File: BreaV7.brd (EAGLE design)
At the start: 30.8 x 19 mm, 32 parts, among them J2 XF2L-0535-1, J3 XF2L-0635-1, Q1 ABM-16MHZ, SW1 LS12T2-T, SW2 EVQ11U09K, SW3 ESE31L11T, U2 TPS62200, X1 22-23-2021

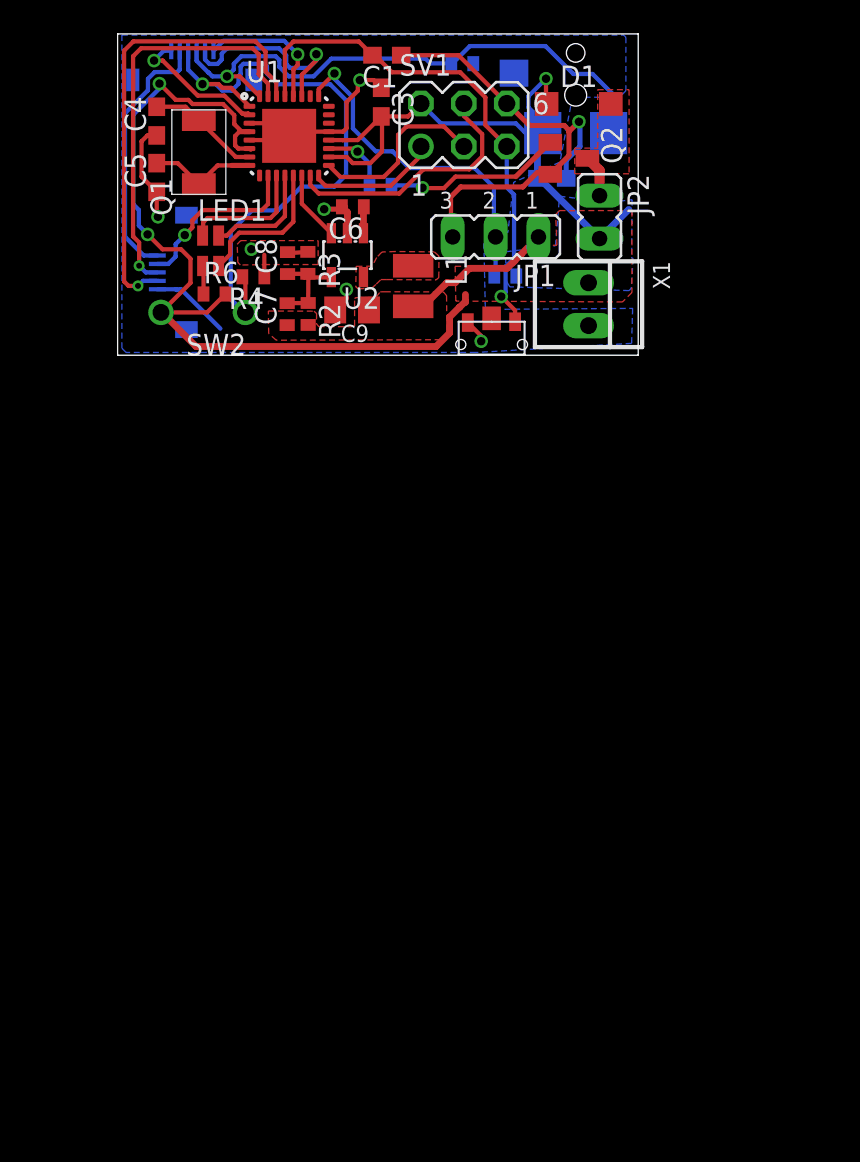
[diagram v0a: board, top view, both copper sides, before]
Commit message: Combined boards
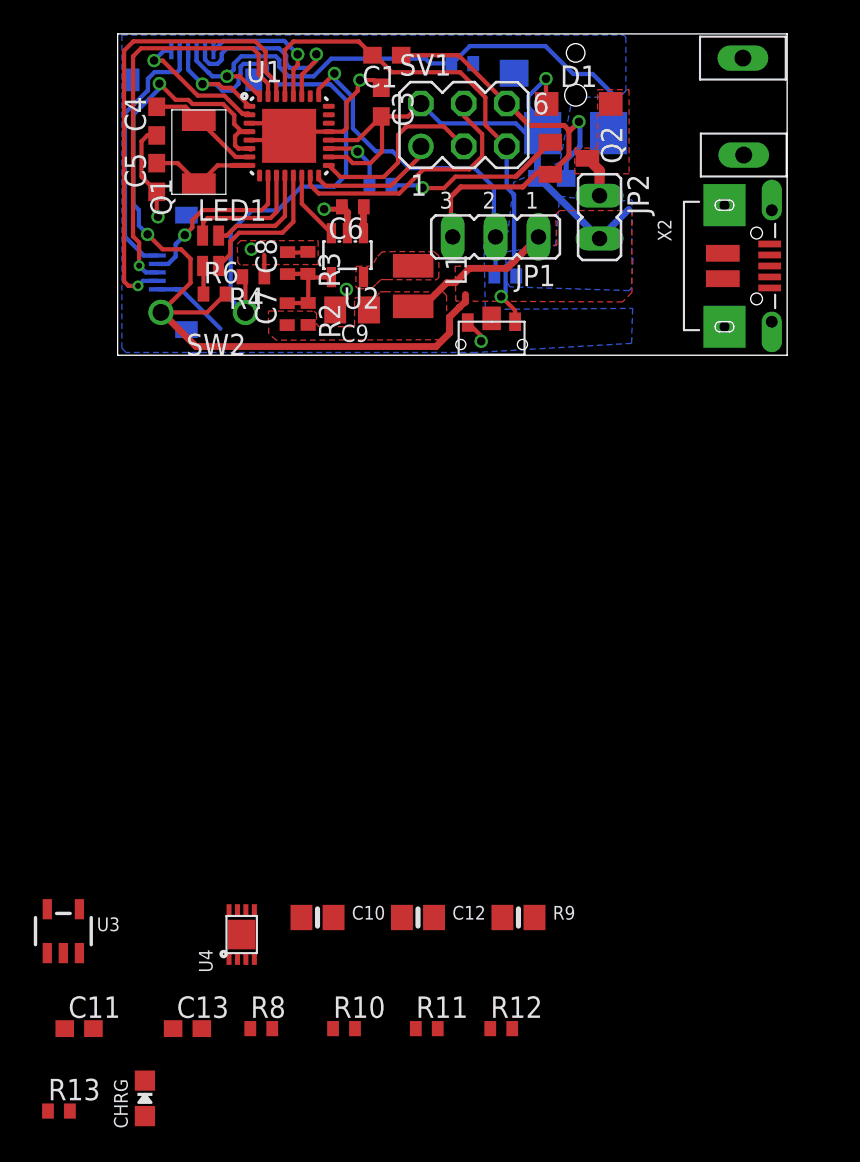
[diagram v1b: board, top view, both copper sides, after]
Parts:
- added C10, C12: 10µF, microbuilder:0805-NO
- added C11: 10nF, rcl:C0603
- added C13: 1uF, rcl:C0603
- added CHRG: ORANGE, microbuilder:CHIPLED_0805_NOOUTLINE
- added R10, R8: 4.7K, resistor:R0402
- added R11: 1K, resistor:R0402
- added R12: 180, resistor:R0402
- added R13: 470, resistor:R0402
- added R9: 2K, microbuilder:0805-NO
- added U3: MCP73831T-2ACI/OT, microbuilder:SOT23-5
- added U4: MAX17044, NewPart:TDFN
- added X2: MicroB, microbuilder:4UCONN_20329
- added X3: CON-1PIN, NewPart:CON-1PIN
- X1: value 22-23-2021 -> CON-1PIN; device con-molex:22-23-2021 -> NewPart:CON-1PIN
- moved X1 17.2 mm to (37.0, 17.6), turned to 90 degrees
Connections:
- new net N$11: CHRG.C, U3.1
- new net N$14: R9.1, U3.5
- new net N$4: C13.1, R11.2, U4.2
- new net N$6: C11.1, R12.2, U4.3
- new net N$8: CHRG.A, R13.2
- new net VBUS1: C10.1, R13.1, U3.4, X2.VBUS
- net GND: now also C10.2, C11.2, C12.2, C13.2, R9.2, U3.2, U4.1, U4.4, U4.6, U4.9, X2.BASE@1, X2.BASE@2, X2.GND, X2.SPRT@1, X2.SPRT@2, X2.SPRT@3, X2.SPRT@4, X3.P$1; no longer X1.2
- net SCL: now also R10.1, U4.7
- net SDA: now also R8.1, U4.8
- net VBAT: now also C12.1, R10.2, R11.1, R12.1, R8.2, U3.3, X1.P$1
- net VCC: no longer X1.1
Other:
- board size 30.8 x 19 mm -> 39.6 x 19 mm

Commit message: 4-layer board
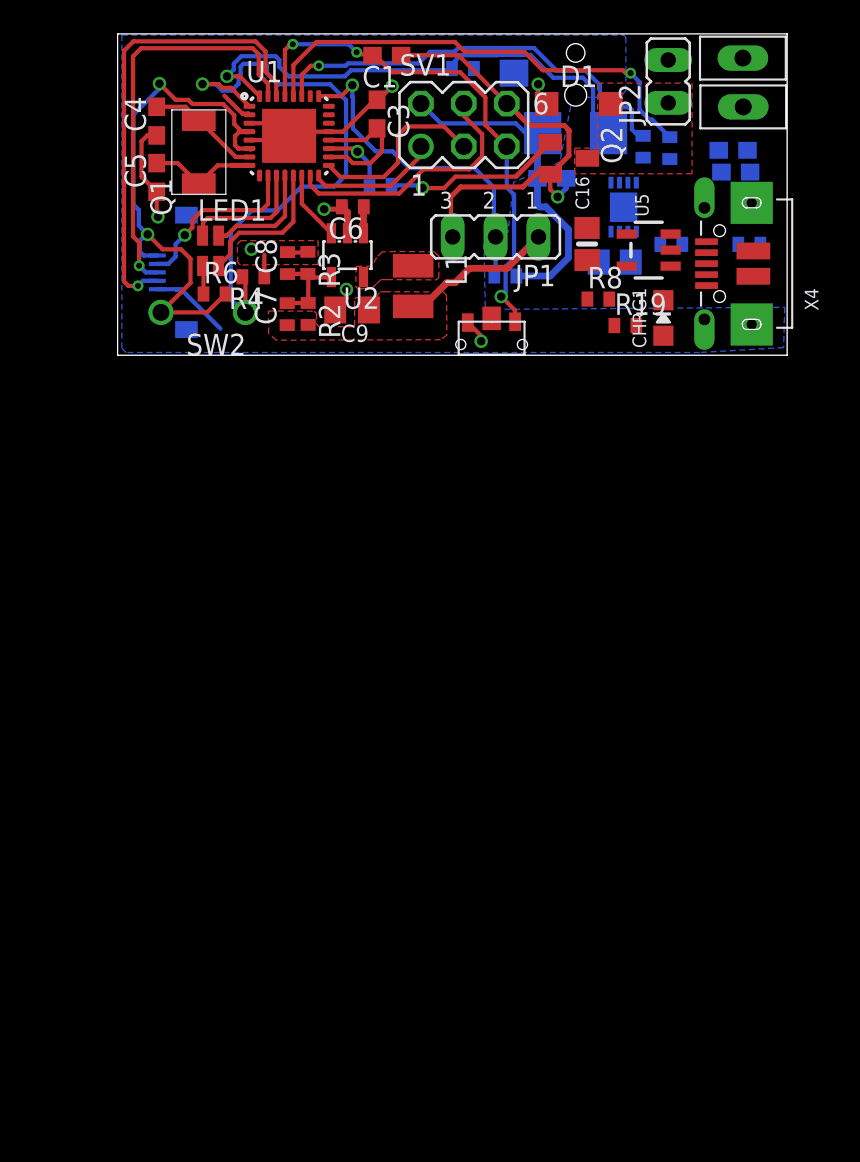
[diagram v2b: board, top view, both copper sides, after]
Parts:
- removed C10, C12: 10µF, microbuilder:0805-NO
- removed C11: 10nF, rcl:C0603
- removed C13: 1uF, rcl:C0603
- removed CHRG: ORANGE, microbuilder:CHIPLED_0805_NOOUTLINE
- removed J3: XF2L-0635-1, con-omron:XF2L-0635-1
- removed R10: 4.7K, resistor:R0402
- removed R11: 1K, resistor:R0402
- removed R12: 180, resistor:R0402
- removed R13: 470, resistor:R0402
- removed R9: 2K, microbuilder:0805-NO
- removed U3: MCP73831T-2ACI/OT, microbuilder:SOT23-5
- removed U4: MAX17044, NewPart:TDFN
- removed X2: MicroB, microbuilder:4UCONN_20329
- added C14, C16: 10µF, microbuilder:0805-NO
- added C15: 10nF, rcl:C0603
- added C17: 1uF, rcl:C0603
- added CHRG1: ORANGE, microbuilder:CHIPLED_0805_NOOUTLINE
- added R15, R16: 4.7K, resistor:R0402
- added R17: 1K, resistor:R0402
- added R18: 180, resistor:R0402
- added R19: 470, resistor:R0402
- added U5: MCP73831T-2ACI/OT, microbuilder:SOT23-5
- added U6: MAX17044, NewPart:TDFN
- added X4: MicroB, microbuilder:4UCONN_20329
- R8: value 4.7K -> 2K
- moved R8 47.6 mm to (28.5, 3.29)
- moved JP2 9.00 mm to (32.6, 16.2), turned to 0 degrees
- moved X3 2.85 mm to (37.0, 14.7)
- moved C3 0.75 mm to (15.4, 14.2)
- moved R7 0.29 mm to (20.5, 16.9)
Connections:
- removed net N$11: CHRG.C, U3.1
- removed net N$14: R9.1, U3.5
- removed net N$4: C13.1, R11.2, U4.2
- removed net N$6: C11.1, R12.2, U4.3
- removed net N$8: CHRG.A, R13.2
- removed net VBAT: C12.1, J2.1, J3.5, R10.2, R11.1, R12.1, R8.2, U3.3, X1.P$1
- removed net VBUS1: C10.1, R13.1, U3.4, X2.VBUS
- new net N$12: R8.1, U5.5
- new net N$13: C17.1, R17.2, U6.2
- new net N$15: C15.1, R18.2, U6.3
- new net N$16: CHRG1.A, R19.2
- new net N$17: CHRG1.C, U5.1
- new net VBUS2: C14.1, R19.1, U5.4, X4.VBUS
- net DETSW: no longer J3.3
- net GND: now also C14.2, C15.2, C16.2, C17.2, R8.2, U5.2, U6.1, U6.4, U6.6, U6.9, X4.BASE@1, X4.BASE@2, X4.GND, X4.SPRT@1, X4.SPRT@2, X4.SPRT@3, X4.SPRT@4; no longer C10.2, C11.2, C12.2, C13.2, R9.2, U3.2, U4.1, U4.4, U4.6, U4.9, X2.BASE@1, X2.BASE@2, X2.GND, X2.SPRT@1, X2.SPRT@2, X2.SPRT@3, X2.SPRT@4
- net LEDSOC: no longer J3.6
- net PWRSW: no longer J3.4
- net SCL: now also R16.1, U6.7; no longer J3.1, R10.1, U4.7
- net SDA: now also R15.1, U6.8; no longer J3.2, R8.1, U4.8
- net VCC: now also C16.1, J2.1, R15.2, R16.2, R17.1, R18.1, U5.3, X1.P$1
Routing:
- net VCC: track 87.6 -> 63.5 mm
- net SCL: track 8.14 -> 28.0 mm
- net VBAT: track 15.5 -> 0.00 mm
- net SDA: track 12.0 -> 25.4 mm
- net LEDSOC: track 8.24 -> 1.96 mm, vias 1 -> 0
- net DETSW: track 34.0 -> 30.5 mm
- net GND: track 61.7 -> 59.1 mm
- net N$9: track 2.51 -> 0.00 mm
- net PWRSW: track 36.6 -> 34.3 mm
- net N$3: track 20.6 -> 20.0 mm
- net RST: track 30.9 -> 30.7 mm, vias 1 -> 3
- added copper zone on layer 2, net GND
- added copper zone on layer 15, net VCC
- removed copper zone on layer 1, net VCC
- removed copper zone on layer 16, net VCC
